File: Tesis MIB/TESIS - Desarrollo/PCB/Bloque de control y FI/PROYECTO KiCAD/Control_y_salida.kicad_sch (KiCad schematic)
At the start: 30 parts, among them J5 FSR_b, J6 FSR_a, Q1 BF422, Q2 BF421, Q3 BF557, Q4 BC547, Q5 BF421, Q6 BF422, SW1 Decr, SW2 Inc, SW3 Acept, U1 LCD-016N002L, U2 PSoC4_kit049_(CY8C4245AXI-483), U3 TL082

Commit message: Actualiza avances
Se incorporan varios artículos de referencia y se actualiza el documento de Tesis con el Cap 1 (pag. 19 a 39).
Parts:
- Q1, Q6: value BF422 -> BF471
- Q3: value BF557 -> BF421
- Q4: value BC547 -> BF471
- R10: value 3k3 -> 2k
- RV3: value 10k -> 50k
- RV4: value 5k -> 10k
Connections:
- net Iout: now also Q5.2 (C), Q6.2 (C); no longer Q5.1 (C), Q6.1 (C)
- net VCC: now also Q3.1 (E), Q5.1 (E); no longer Q3.3 (E), Q5.3 (E)
- net VEE: now also Q4.1 (E), Q6.1 (E); no longer Q4.3 (E), Q6.3 (E)
- net at D2.1 (K): now also R9.2; no longer R10.2
- net at D1.1 (K), D2.2 (A), U3.2 (-): now also Q1.1 (E), Q2.1 (E); no longer Q1.3 (E), Q2.3 (E)
- net at D1.2 (A): now also R10.2; no longer R9.2
- new net: Q1.2 (C), Q3.2 (C), Q3.3 (B), Q5.3 (B)
- new net: Q1.3 (B), Q2.3 (B), U3.1
- new net: Q2.2 (C), Q4.2 (C), Q4.3 (B), Q6.3 (B)
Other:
- moved on the sheet: D1, D2, J5, J6, Q1, Q5, R10, R4, R5, R6, R7, R8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

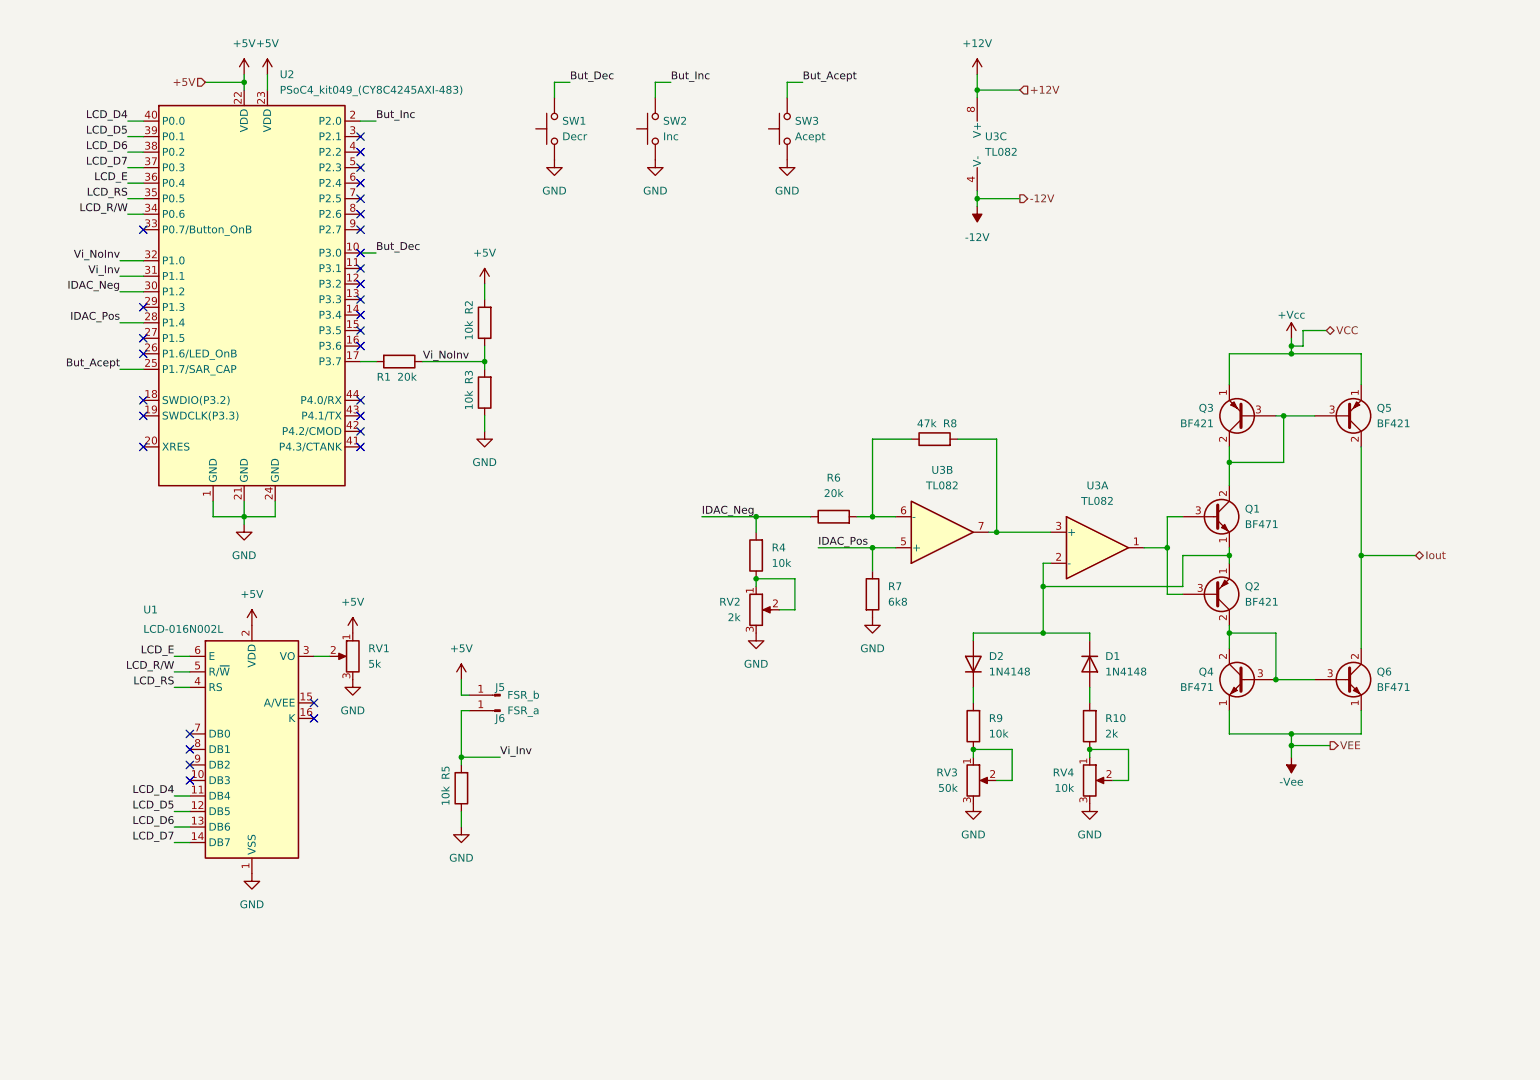
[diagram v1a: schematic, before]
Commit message: Acualización del CAP2
Finalización de la 1ra parte del CAP2, redacción de titulos y subtitulos para esquematizar los CAP3 y CAP4, actualización de los indices de Contenidos, Tablas y Figuras y Referencias insertadas (hasta la 48).
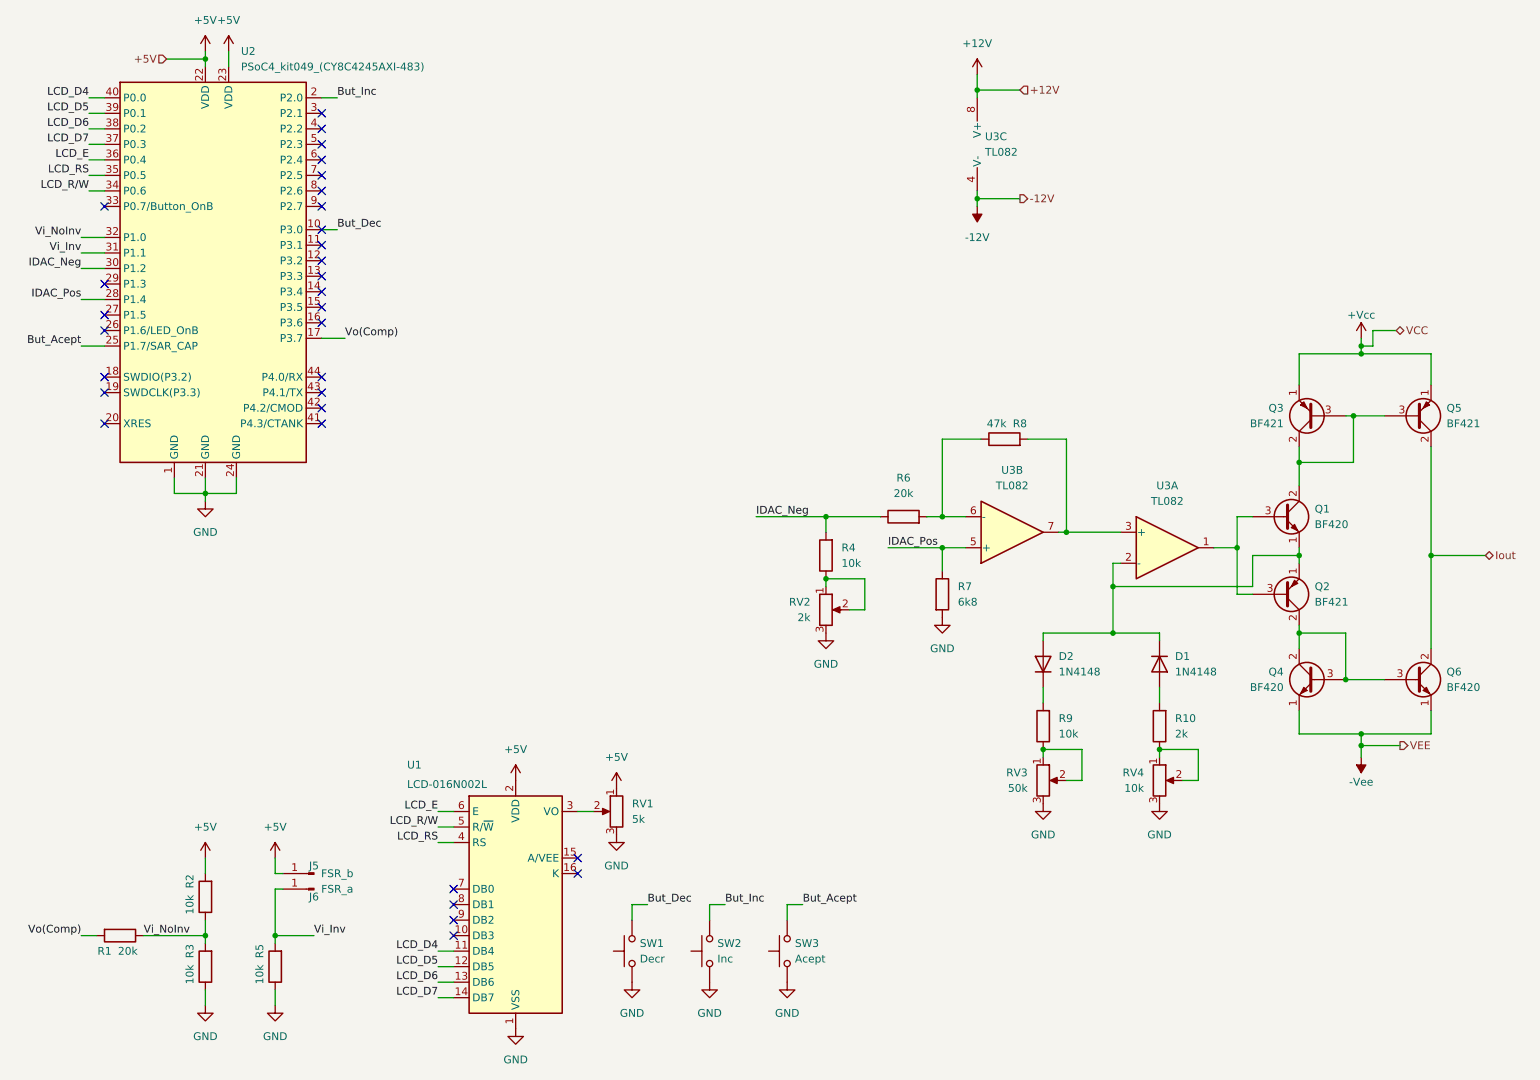
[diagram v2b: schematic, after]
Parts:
- Q1, Q4, Q6: value BF471 -> BF420
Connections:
- net Vo(Comp): now reaches R1.2, U2.17 (P3.7)
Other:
- moved on the sheet: D1, D2, J5, J6, Q1, Q2, Q3, Q4, Q5, Q6, R1, R10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

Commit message: Actualiza Pruebas
Agrega planilla, gráficos y capturas del osciloscopio para el CAP3
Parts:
- added R10, R11, R2, R3: 390, Resistor_THT:R_Axial_DIN0207_L6.3mm_D2.5mm_P10.16mm_Horizontal, symbol Device:R
- renumbered D2 to D1, D1 to D2, Q3 to Q1, Q5 to Q2, Q1 to Q3, Q2 to Q4, Q4 to Q5, R2 to R12, R1 to R13, R3 to R14, R5 to R15, R8 to R4, R6 to R5, R4 to R6, R9 to R8, R10 to R9, RV2 to RV1, RV3 to RV2, RV4 to RV3, RV1 to RV4, U3 to U1, U1 to U3
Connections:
- net VCC: now also R2.2, R3.2; no longer Q1.1 (E), Q2.1 (E)
- net VEE: now also R10.1, R11.1; no longer Q5.1 (E), Q6.1 (E)
- new net: Q5.1 (E), R10.2
- new net: Q1.1 (E), R2.1
- new net: Q2.1 (E), R3.1
- new net: Q6.1 (E), R11.2
